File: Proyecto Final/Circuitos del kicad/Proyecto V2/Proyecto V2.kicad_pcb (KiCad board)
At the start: 2 copper layers, 265 x 174.5 mm, 43 parts, among them J1 12v, Q1 PN2222A, Q2 PN2222A, Q3 PN2222A, SW1 SW_Push, SW2 SW_Push, SW3 SW_Push, SW4 SW_Push, U1 LM7805, U3 ATmega328P-P, Y1 16MHz

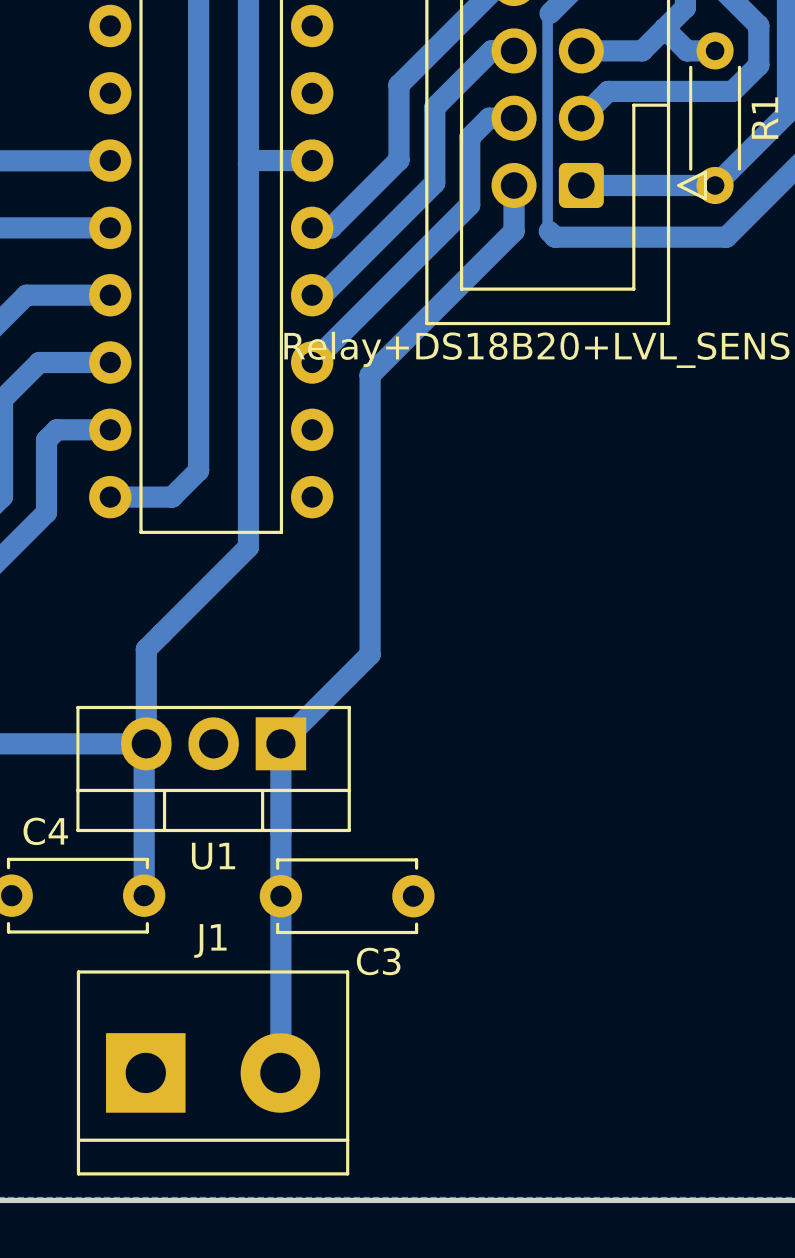
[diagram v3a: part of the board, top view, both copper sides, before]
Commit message: pistas mas anchas
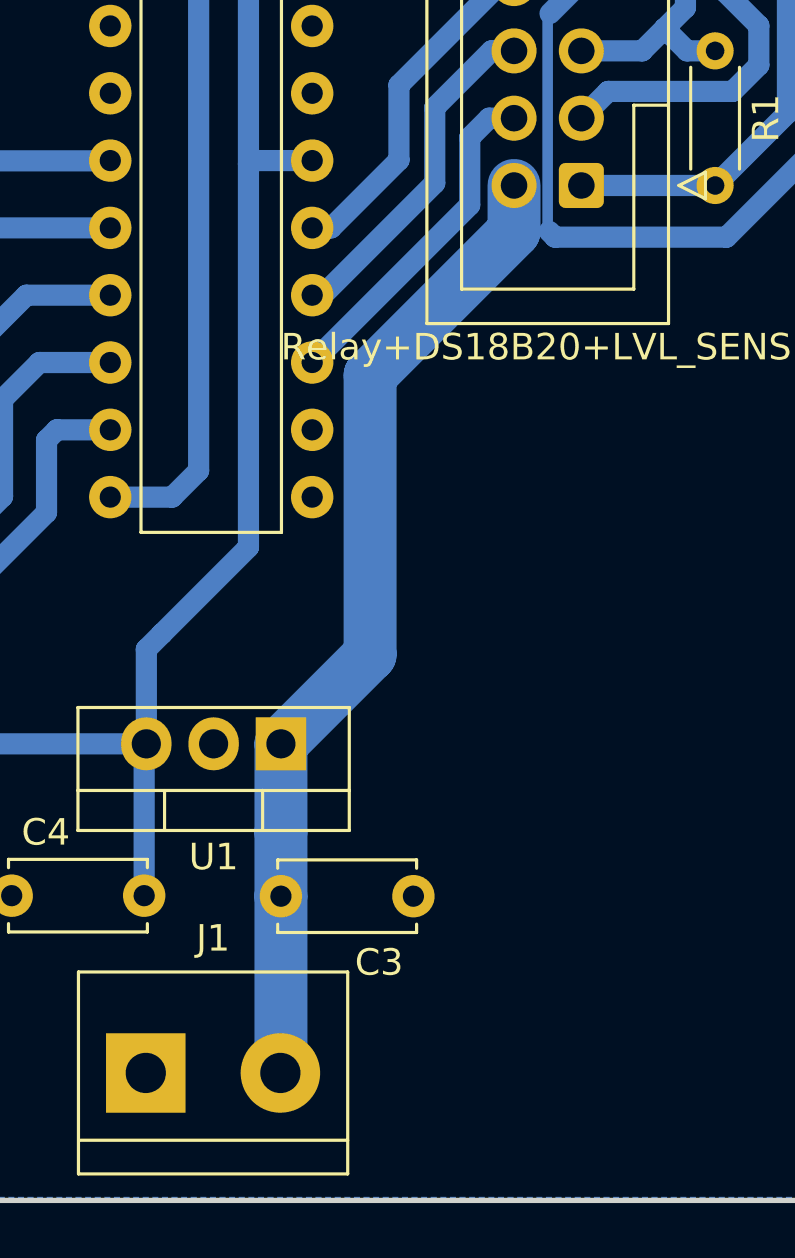
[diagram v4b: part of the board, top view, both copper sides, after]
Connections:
- Encoder/puls-arduino1 pad 7: Net-(Encoder/puls-arduino1-Pad7) -> +12V
- U3 pad 23: Net-(Encoder/puls-arduino1-Pad7) -> +12V
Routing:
- net Net-(Encoder/puls-arduino1-Pad7): track 166.1 -> 0.00 mm
- net +12V: track 210.9 -> 377.1 mm
